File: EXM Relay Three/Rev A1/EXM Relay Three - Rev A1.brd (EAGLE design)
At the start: 80 x 50 mm, 24 parts, among them J1 MSTBA3, J10 MSTBA2, J2 MSTBA3, J3 22-05-7038-03, J4 22-05-7038-03, J5 22-05-7038-03, J6 22-05-7038-03, J7 MSTBA3, J8 22-05-7038-03, J9 22-05-7038-03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

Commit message: Clean the folder and repair .sch file
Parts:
- moved K3 1.00 mm to (65.0, 24.0)
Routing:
- net SIG_IN_3: track 17.1 -> 18.1 mm
- net SIG3_2_NO: track 22.8 -> 23.8 mm
- net SIG3_2_NC: track 13.4 -> 12.4 mm
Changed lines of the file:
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@@
 <layer number="46" name="Milling" color="3" fill="1" visible="no" active="yes"/>
 <layer number="47" name="Measures" color="7" fill="1" visible="no" active="yes"/>
-<layer number="48" name="Document" color="7" fill="1" visible="no" active="yes"/>
+<layer number="48" name="Document" color="7" fill="1" visible="yes" active="yes"/>
 <layer number="49" name="Reference" color="7" fill="1" visible="no" active="yes"/>
 <layer number="50" name="dxf" color="7" fill="1" visible="no" active="yes"/>
@@
 <text x="28.8" y="39.8" size="1.016" layer="21" align="center">SIG</text>
 <text x="10.9" y="39.9" size="1.016" layer="21" align="center">GND</text>
-<text x="23.6" y="6.7" size="1.016" layer="21" rot="R90" align="center-left">NC2</text>
-<text x="21" y="6.7" size="1.016" layer="21" rot="R90" align="center-left">NO2</text>
+<text x="14.6" y="6.7" size="1.016" layer="21" rot="R90" align="center-left">NC2</text>
+<text x="12" y="6.7" size="1.016" layer="21" rot="R90" align="center-left">NO2</text>
 <text x="18.4" y="6.7" size="1.016" layer="21" rot="R90" align="center-left">GND</text>
-<text x="14.6" y="6.7" size="1.016" layer="21" rot="R90" align="center-left">NC1</text>
-<text x="12" y="6.7" size="1.016" layer="21" rot="R90" align="center-left">NO1</text>
+<text x="23.6" y="6.7" size="1.016" layer="21" rot="R90" align="center-left">NC1</text>
+<text x="21" y="6.7" size="1.016" layer="21" rot="R90" align="center-left">NO1</text>
 <text x="9.4" y="6.7" size="1.016" layer="21" rot="R90" align="center-left">GND</text>
 <text x="33.9" y="39.8" size="1.016" layer="21" align="center">+24V</text>
@@
 <text x="68.7" y="39.8" size="1.016" layer="21" align="center">+24V</text>
 <text x="58.4" y="39.8" size="1.016" layer="21" align="center">GND</text>
-<text x="46.6" y="6.7" size="1.016" layer="21" rot="R90" align="center-left">NC2</text>
-<text x="44" y="6.7" size="1.016" layer="21" rot="R90" align="center-left">NO2</text>
+<text x="37.6" y="6.7" size="1.016" layer="21" rot="R90" align="center-left">NC2</text>
+<text x="35" y="6.7" size="1.016" layer="21" rot="R90" align="center-left">NO2</text>
 <text x="41.4" y="6.7" size="1.016" layer="21" rot="R90" align="center-left">GND</text>
-<text x="37.6" y="6.7" size="1.016" layer="21" rot="R90" align="center-left">NC1</text>
-<text x="35" y="6.7" size="1.016" layer="21" rot="R90" align="center-left">NO1</text>
+<text x="46.6" y="6.7" size="1.016" layer="21" rot="R90" align="center-left">NC1</text>
+<text x="44" y="6.7" size="1.016" layer="21" rot="R90" align="center-left">NO1</text>
 <text x="32.4" y="6.7" size="1.016" layer="21" rot="R90" align="center-left">GND</text>
-<text x="70.6" y="6.7" size="1.016" layer="21" rot="R90" align="center-left">NC2</text>
-<text x="68" y="6.7" size="1.016" layer="21" rot="R90" align="center-left">NO2</text>
+<text x="61.6" y="6.7" size="1.016" layer="21" rot="R90" align="center-left">NC2</text>
+<text x="59" y="6.7" size="1.016" layer="21" rot="R90" align="center-left">NO2</text>
 <text x="65.4" y="6.7" size="1.016" layer="21" rot="R90" align="center-left">GND</text>
-<text x="61.6" y="6.7" size="1.016" layer="21" rot="R90" align="center-left">NC1</text>
-<text x="59" y="6.7" size="1.016" layer="21" rot="R90" align="center-left">NO1</text>
+<text x="70.6" y="6.7" size="1.016" layer="21" rot="R90" align="center-left">NC1</text>
+<text x="68" y="6.7" size="1.016" layer="21" rot="R90" align="center-left">NO1</text>
 <text x="56.4" y="6.7" size="1.016" layer="21" rot="R90" align="center-left">GND</text>
 </plain>
@@
 <attribute name="OC_NEWARK" value="71C4162" x="63.6" y="-17" size="1.778" layer="27" rot="R180" display="off"/>
 </element>
-<element name="K3" library="rel-omron" package="PY08" value="MY2" x="64" y="24" rot="R180"/>
+<element name="K3" library="rel-omron" package="PY08" value="MY2" x="65" y="24" rot="R180"/>
 <element name="J8" library="con-molex" package="7395-03" value="22-05-7038-03" x="68" y="5">
 <attribute name="MPN" value="" x="7" y="49" size="1.778" layer="27" display="off"/>
@@
 <contactref element="J8" pad="1"/>
 <contactref element="K3" pad="4"/>
-<wire x1="70.54" y1="5" x2="70.605" y2="5.065" width="0.8128" layer="1"/>
-<wire x1="70.605" y1="5.065" x2="70.605" y2="15.325" width="0.8128" layer="1"/>
+<wire x1="70.54" y1="5" x2="70.54" y2="14.26" width="0.8128" layer="1"/>
+<wire x1="70.54" y1="14.26" x2="71.605" y2="15.325" width="0.8128" layer="1"/>
 </signal>
 <signal name="SIG3_1_NO">
 <contactref element="J8" pad="2"/>
 <contactref element="K3" pad="8"/>
-<wire x1="68" y1="5" x2="68" y2="14" width="0.8128" layer="1"/>
-<wire x1="68" y1="14" x2="67" y2="15" width="0.8128" layer="1"/>
-<wire x1="67" y1="15" x2="67" y2="17" width="0.8128" layer="1"/>
-<wire x1="67" y1="17" x2="69.425" y2="19.425" width="0.8128" layer="1"/>
-<wire x1="69.425" y1="19.425" x2="70.605" y2="19.425" width="0.8128" layer="1"/>
+<wire x1="68" y1="5" x2="68" y2="18" width="0.8128" layer="1"/>
+<wire x1="69.425" y1="19.425" x2="71.605" y2="19.425" width="0.8128" layer="1"/>
+<wire x1="68" y1="18" x2="69.425" y2="19.425" width="0.8128" layer="1"/>
 </signal>
 <signal name="SIG3_2_NC">
@@
 <wire x1="61.54" y1="5" x2="61.54" y2="13.46" width="0.8128" layer="1"/>
 <wire x1="61.54" y1="13.46" x2="59.675" y2="15.325" width="0.8128" layer="1"/>
-<wire x1="59.675" y1="15.325" x2="57.405" y2="15.325" width="0.8128" layer="1"/>
+<wire x1="59.675" y1="15.325" x2="58.405" y2="15.325" width="0.8128" layer="1"/>
 </signal>
 <signal name="SIG3_2_NO">
@@
 <wire x1="53" y1="12" x2="53" y2="18" width="0.8128" layer="1"/>
 <wire x1="53" y1="18" x2="54.425" y2="19.425" width="0.8128" layer="1"/>
-<wire x1="54.425" y1="19.425" x2="57.405" y2="19.425" width="0.8128" layer="1"/>
+<wire x1="54.425" y1="19.425" x2="58.405" y2="19.425" width="0.8128" layer="1"/>
 </signal>
 <signal name="SIG_IN_3">
 <contactref element="J7" pad="2"/>
 <contactref element="K3" pad="14"/>
-<wire x1="70.605" y1="32.075" x2="64.925" y2="32.075" width="0.8128" layer="1"/>
+<wire x1="71.605" y1="32.075" x2="64.925" y2="32.075" width="0.8128" layer="1"/>
 <wire x1="64.925" y1="32.075" x2="63.6" y2="33.4" width="0.8128" layer="1"/>
 <wire x1="63.6" y1="33.4" x2="63.6" y2="42.92" width="0.8128" layer="1"/>

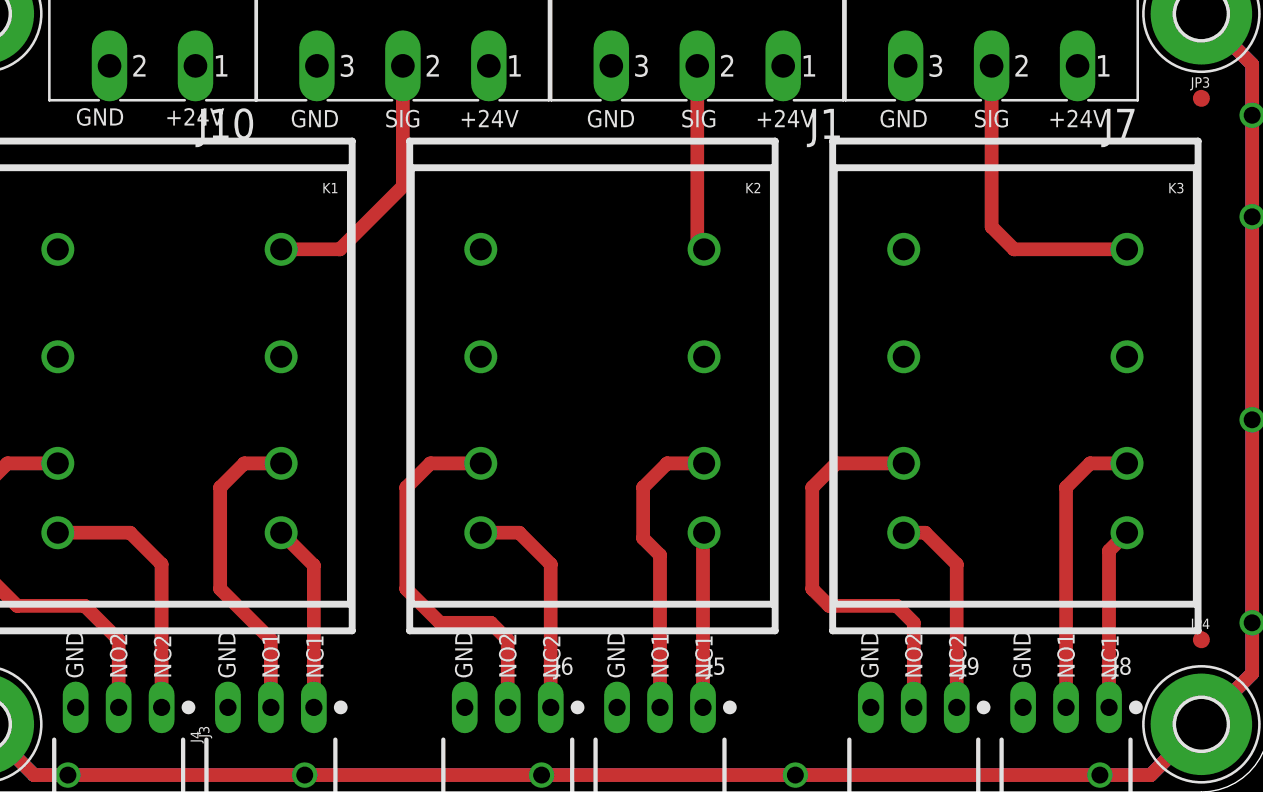
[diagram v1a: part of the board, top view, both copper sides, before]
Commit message: Renumber outputs and change silkscreen
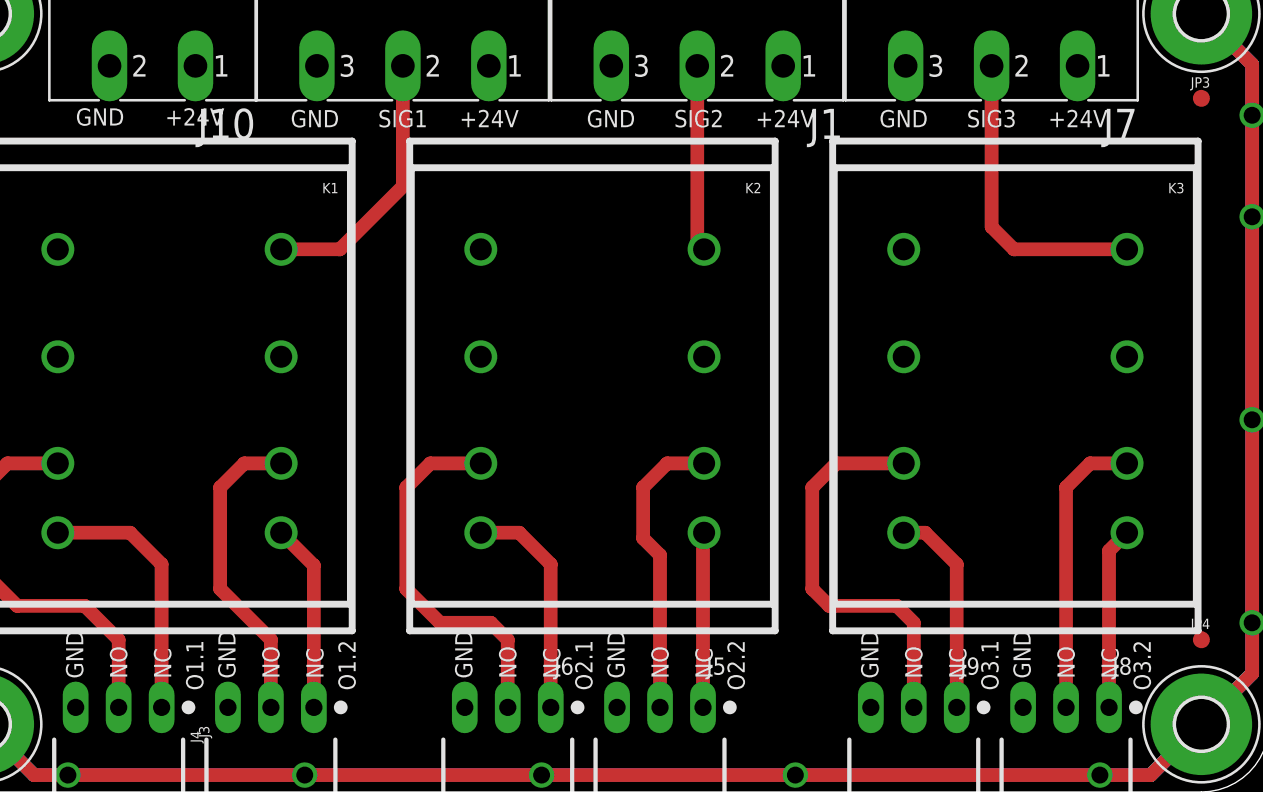
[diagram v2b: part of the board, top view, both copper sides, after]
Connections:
- net SIG1_1_NC: now also J3.1, K1.1; no longer J4.1, K1.4
- net SIG1_1_NO: now also J3.2, K1.5; no longer J4.2, K1.8
- net SIG1_2_NC: now also J4.1, K1.4; no longer J3.1, K1.1
- net SIG1_2_NO: now also J4.2, K1.8; no longer J3.2, K1.5
- net SIG2_1_NC: now also J6.1, K2.1; no longer J5.1, K2.4
- net SIG2_1_NO: now also J6.2, K2.5; no longer J5.2, K2.8
- net SIG2_2_NC: now also J5.1, K2.4; no longer J6.1, K2.1
- net SIG2_2_NO: now also J5.2, K2.8; no longer J6.2, K2.5
- net SIG3_1_NC: now also J9.1, K3.1; no longer J8.1, K3.4
- net SIG3_1_NO: now also J9.2, K3.5; no longer J8.2, K3.8
- net SIG3_2_NC: now also J8.1, K3.4; no longer J9.1, K3.1
- net SIG3_2_NO: now also J8.2, K3.8; no longer J9.2, K3.5
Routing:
- net SIG3_2_NO: track 23.8 -> 17.2 mm
- net SIG3_1_NO: track 17.2 -> 23.8 mm
- net SIG1_2_NO: track 23.7 -> 18.4 mm
- net SIG1_1_NO: track 18.4 -> 23.7 mm
- net SIG2_2_NO: track 22.2 -> 17.6 mm
- net SIG2_1_NO: track 17.6 -> 22.2 mm
- net SIG1_2_NC: track 15.4 -> 11.1 mm
- net SIG1_1_NC: track 11.1 -> 15.4 mm
- net SIG2_2_NC: track 13.4 -> 10.4 mm
- net SIG2_1_NC: track 10.4 -> 13.4 mm
- net SIG3_2_NC: track 12.4 -> 10.8 mm
- net SIG3_1_NC: track 10.8 -> 12.4 mm
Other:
- board text added: "NC"
- board text added: "NO"
- board text added: "O1.1"
- board text added: "O1.2"
- board text added: "O2.1"
- board text added: "O2.2"
- board text added: "O3.1"
- board text added: "O3.2"
- board text added: "SIG1"
- board text added: "SIG2"
- board text added: "SIG3"
- board text removed: "NC1"
- board text removed: "NC2"
- board text removed: "NO1"
- board text removed: "NO2"
- board text removed: "SIG"
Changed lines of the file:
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@@
 RevA1</text>
 <text x="16.5" y="39.9" size="1.016" layer="21" align="center">+24V</text>
-<text x="28.8" y="39.8" size="1.016" layer="21" align="center">SIG</text>
+<text x="28.8" y="39.8" size="1.016" layer="21" align="center">SIG1</text>
 <text x="10.9" y="39.9" size="1.016" layer="21" align="center">GND</text>
-<text x="14.6" y="6.7" size="1.016" layer="21" rot="R90" align="center-left">NC2</text>
-<text x="12" y="6.7" size="1.016" layer="21" rot="R90" align="center-left">NO2</text>
+<text x="14.6" y="6.7" size="1.016" layer="21" rot="R90" align="center-left">NC</text>
+<text x="12" y="6.7" size="1.016" layer="21" rot="R90" align="center-left">NO</text>
 <text x="18.4" y="6.7" size="1.016" layer="21" rot="R90" align="center-left">GND</text>
-<text x="23.6" y="6.7" size="1.016" layer="21" rot="R90" align="center-left">NC1</text>
-<text x="21" y="6.7" size="1.016" layer="21" rot="R90" align="center-left">NO1</text>
+<text x="23.6" y="6.7" size="1.016" layer="21" rot="R90" align="center-left">NC</text>
+<text x="21" y="6.7" size="1.016" layer="21" rot="R90" align="center-left">NO</text>
 <text x="9.4" y="6.7" size="1.016" layer="21" rot="R90" align="center-left">GND</text>
 <text x="33.9" y="39.8" size="1.016" layer="21" align="center">+24V</text>
 <text x="23.6" y="39.8" size="1.016" layer="21" align="center">GND</text>
-<text x="46.3" y="39.8" size="1.016" layer="21" align="center">SIG</text>
+<text x="46.3" y="39.8" size="1.016" layer="21" align="center">SIG2</text>
 <text x="51.4" y="39.8" size="1.016" layer="21" align="center">+24V</text>
 <text x="41.1" y="39.8" size="1.016" layer="21" align="center">GND</text>
-<text x="63.6" y="39.8" size="1.016" layer="21" align="center">SIG</text>
+<text x="63.6" y="39.8" size="1.016" layer="21" align="center">SIG3</text>
 <text x="68.7" y="39.8" size="1.016" layer="21" align="center">+24V</text>
 <text x="58.4" y="39.8" size="1.016" layer="21" align="center">GND</text>
-<text x="37.6" y="6.7" size="1.016" layer="21" rot="R90" align="center-left">NC2</text>
-<text x="35" y="6.7" size="1.016" layer="21" rot="R90" align="center-left">NO2</text>
+<text x="37.6" y="6.7" size="1.016" layer="21" rot="R90" align="center-left">NC</text>
+<text x="35" y="6.7" size="1.016" layer="21" rot="R90" align="center-left">NO</text>
 <text x="41.4" y="6.7" size="1.016" layer="21" rot="R90" align="center-left">GND</text>
-<text x="46.6" y="6.7" size="1.016" layer="21" rot="R90" align="center-left">NC1</text>
-<text x="44" y="6.7" size="1.016" layer="21" rot="R90" align="center-left">NO1</text>
+<text x="46.6" y="6.7" size="1.016" layer="21" rot="R90" align="center-left">NC</text>
+<text x="44" y="6.7" size="1.016" layer="21" rot="R90" align="center-left">NO</text>
 <text x="32.4" y="6.7" size="1.016" layer="21" rot="R90" align="center-left">GND</text>
-<text x="61.6" y="6.7" size="1.016" layer="21" rot="R90" align="center-left">NC2</text>
-<text x="59" y="6.7" size="1.016" layer="21" rot="R90" align="center-left">NO2</text>
+<text x="61.6" y="6.7" size="1.016" layer="21" rot="R90" align="center-left">NC</text>
+<text x="59" y="6.7" size="1.016" layer="21" rot="R90" align="center-left">NO</text>
 <text x="65.4" y="6.7" size="1.016" layer="21" rot="R90" align="center-left">GND</text>
-<text x="70.6" y="6.7" size="1.016" layer="21" rot="R90" align="center-left">NC1</text>
-<text x="68" y="6.7" size="1.016" layer="21" rot="R90" align="center-left">NO1</text>
+<text x="70.6" y="6.7" size="1.016" layer="21" rot="R90" align="center-left">NC</text>
+<text x="68" y="6.7" size="1.016" layer="21" rot="R90" align="center-left">NO</text>
 <text x="56.4" y="6.7" size="1.016" layer="21" rot="R90" align="center-left">GND</text>
+<text x="16.5" y="6" size="1.016" layer="21" rot="R90" align="center-left">O1.1</text>
+<text x="25.5" y="6" size="1.016" layer="21" rot="R90" align="center-left">O1.2</text>
+<text x="39.5" y="6" size="1.016" layer="21" rot="R90" align="center-left">O2.1</text>
+<text x="48.5" y="6" size="1.016" layer="21" rot="R90" align="center-left">O2.2</text>
+<text x="63.5" y="6" size="1.016" layer="21" rot="R90" align="center-left">O3.1</text>
+<text x="72.5" y="6" size="1.016" layer="21" rot="R90" align="center-left">O3.2</text>
 </plain>
 <attributes>
@@
 <wire x1="46.2" y1="32.48" x2="46.2" y2="42.92" width="0.8128" layer="1"/>
 </signal>
-<signal name="SIG2_1_NO">
-<contactref element="J5" pad="2"/>
-<contactref element="K2" pad="8"/>
-<wire x1="44" y1="5" x2="44" y2="14" width="0.8128" layer="1"/>
-<wire x1="44" y1="14" x2="43" y2="15" width="0.8128" layer="1"/>
-<wire x1="43" y1="15" x2="43" y2="18" width="0.8128" layer="1"/>
-<wire x1="43" y1="18" x2="44.425" y2="19.425" width="0.8128" layer="1"/>
-<wire x1="44.425" y1="19.425" x2="46.605" y2="19.425" width="0.8128" layer="1"/>
-</signal>
-<signal name="SIG1_1_NC">
+<signal name="SIG1_2_NC">
 <contactref element="J4" pad="1"/>
 <contactref element="K1" pad="4"/>
@@
 <wire x1="23.54" y1="13.39" x2="21.605" y2="15.325" width="0.8128" layer="1"/>
 </signal>
-<signal name="SIG2_2_NC">
+<signal name="SIG2_1_NC">
 <contactref element="J6" pad="1"/>
 <contactref element="K2" pad="1"/>
@@
 <wire x1="35.675" y1="15.325" x2="33.405" y2="15.325" width="0.8128" layer="1"/>
 </signal>
-<signal name="SIG2_2_NO">
+<signal name="SIG2_1_NO">
 <contactref element="J6" pad="2"/>
 <contactref element="K2" pad="5"/>
@@
 <wire x1="35" y1="9" x2="35" y2="5" width="0.8128" layer="1"/>
 </signal>
-<signal name="SIG2_1_NC">
+<signal name="SIG2_2_NC">
 <contactref element="J5" pad="1"/>
 <contactref element="K2" pad="4"/>
@@
 <wire x1="28.8" y1="35.8" x2="28.8" y2="42.92" width="0.8128" layer="1"/>
 </signal>
-<signal name="SIG1_1_NO">
+<signal name="SIG1_2_NO">
 <contactref element="J4" pad="2"/>
 <contactref element="K1" pad="8"/>
@@
 <wire x1="19.425" y1="19.425" x2="21.605" y2="19.425" width="0.8128" layer="1"/>
 </signal>
-<signal name="SIG1_2_NO">
+<signal name="SIG1_1_NO">
 <contactref element="J3" pad="2"/>
 <contactref element="K1" pad="5"/>
@@
 <wire x1="5.425" y1="19.425" x2="8.405" y2="19.425" width="0.8128" layer="1"/>
 </signal>
-<signal name="SIG1_2_NC">
+<signal name="SIG1_1_NC">
 <contactref element="J3" pad="1"/>
 <contactref element="K1" pad="1"/>
@@
 <wire x1="14.54" y1="13.46" x2="14.54" y2="5" width="0.8128" layer="1"/>
 </signal>
-<signal name="SIG3_1_NC">
+<signal name="SIG3_2_NC">
 <contactref element="J8" pad="1"/>
 <contactref element="K3" pad="4"/>
@@
 <wire x1="70.54" y1="14.26" x2="71.605" y2="15.325" width="0.8128" layer="1"/>
 </signal>
-<signal name="SIG3_1_NO">
+<signal name="SIG3_2_NO">
 <contactref element="J8" pad="2"/>
 <contactref element="K3" pad="8"/>
@@
 <wire x1="68" y1="18" x2="69.425" y2="19.425" width="0.8128" layer="1"/>
 </signal>
-<signal name="SIG3_2_NC">
+<signal name="SIG3_1_NC">
 <contactref element="J9" pad="1"/>
 <contactref element="K3" pad="1"/>
@@
 <wire x1="59.675" y1="15.325" x2="58.405" y2="15.325" width="0.8128" layer="1"/>
 </signal>
-<signal name="SIG3_2_NO">
+<signal name="SIG3_1_NO">
 <contactref element="J9" pad="2"/>
 <contactref element="K3" pad="5"/>
@@
 <via x="25" y="49" extent="1-16" drill="1"/>
 </signal>
+<signal name="SIG2_2_NO">
+<contactref element="K2" pad="8"/>
+<contactref element="J5" pad="2"/>
+<wire x1="44" y1="5" x2="44" y2="14" width="0.8128" layer="1"/>
+<wire x1="44" y1="14" x2="43" y2="15" width="0.8128" layer="1"/>
+<wire x1="43" y1="15" x2="43" y2="18" width="0.8128" layer="1"/>
+<wire x1="43" y1="18" x2="44.425" y2="19.425" width="0.8128" layer="1"/>
+<wire x1="44.425" y1="19.425" x2="46.605" y2="19.425" width="0.8128" layer="1"/>
+</signal>
 </signals>

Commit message: Generate MDP files
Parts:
- J2: value MSTBA3 -> 22-05-7038-03; device con-phoenix-508:MSTBA3 -> con-molex:7395-03
- J4: value 22-05-7038-03 -> MSTBA3; device con-molex:7395-03 -> con-phoenix-508:MSTBA3
- moved J2 58.2 mm to (68.0, 5.00), turned to 0 degrees
- moved K1 50.0 mm to (65.0, 24.0)
- moved K3 50.0 mm to (15.0, 24.0)
- moved J4 49.8 mm to (46.2, 48.0), turned to 180 degrees
- moved J3 47.0 mm to (59.0, 5.00)
- moved J8 47.0 mm to (21.0, 5.00)
- moved J9 47.0 mm to (12.0, 5.00)
- moved J7 34.8 mm to (28.8, 48.0)
- moved J1 17.4 mm to (63.6, 48.0)
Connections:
- net +24V: now also J4.1; no longer J2.1
- net SIG1_1_NC: now also J9.1, K3.1; no longer J3.1, K1.1
- net SIG1_1_NO: now also J9.2, K3.5; no longer J3.2, K1.5
- net SIG1_2_NC: now also J8.1, K3.4; no longer J4.1, K1.4
- net SIG1_2_NO: now also J8.2, K3.8; no longer J4.2, K1.8
- net SIG3_1_NC: now also J3.1, K1.1; no longer J9.1, K3.1
- net SIG3_1_NO: now also J3.2, K1.5; no longer J9.2, K3.5
- net SIG3_2_NC: now also J2.1, K1.4; no longer J8.1, K3.4
- net SIG3_2_NO: now also J2.2, K1.8; no longer J8.2, K3.8
- net SIG_IN_1: now also J7.2, K3.14; no longer J2.2, K1.14
- net SIG_IN_2: now also J4.2; no longer J1.2
- net SIG_IN_3: now also J1.2, K1.14; no longer J7.2, K3.14
